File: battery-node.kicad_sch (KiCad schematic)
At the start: 20 parts, among them J2 Conn_01x02, J3 Conn_01x02, J7 TC2050, U1 ESP32-H2-MINI-1-H2S

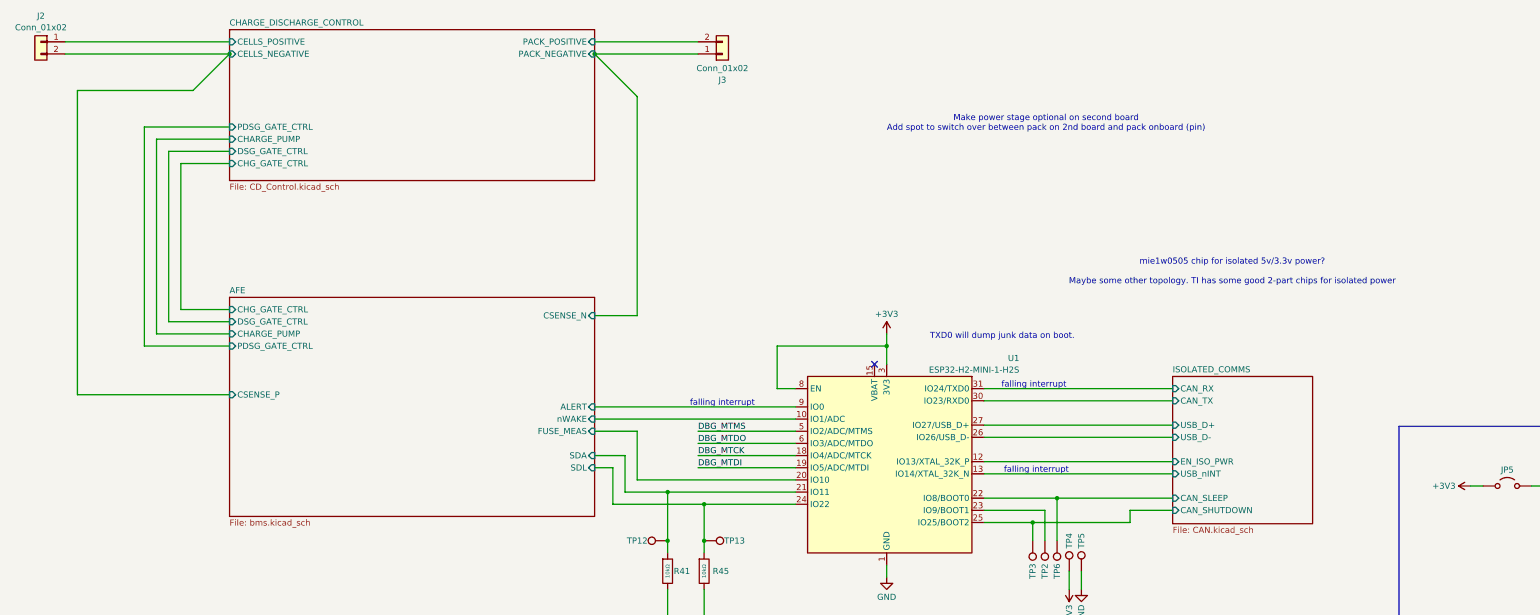
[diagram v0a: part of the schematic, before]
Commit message: prepping for split into 2 boards
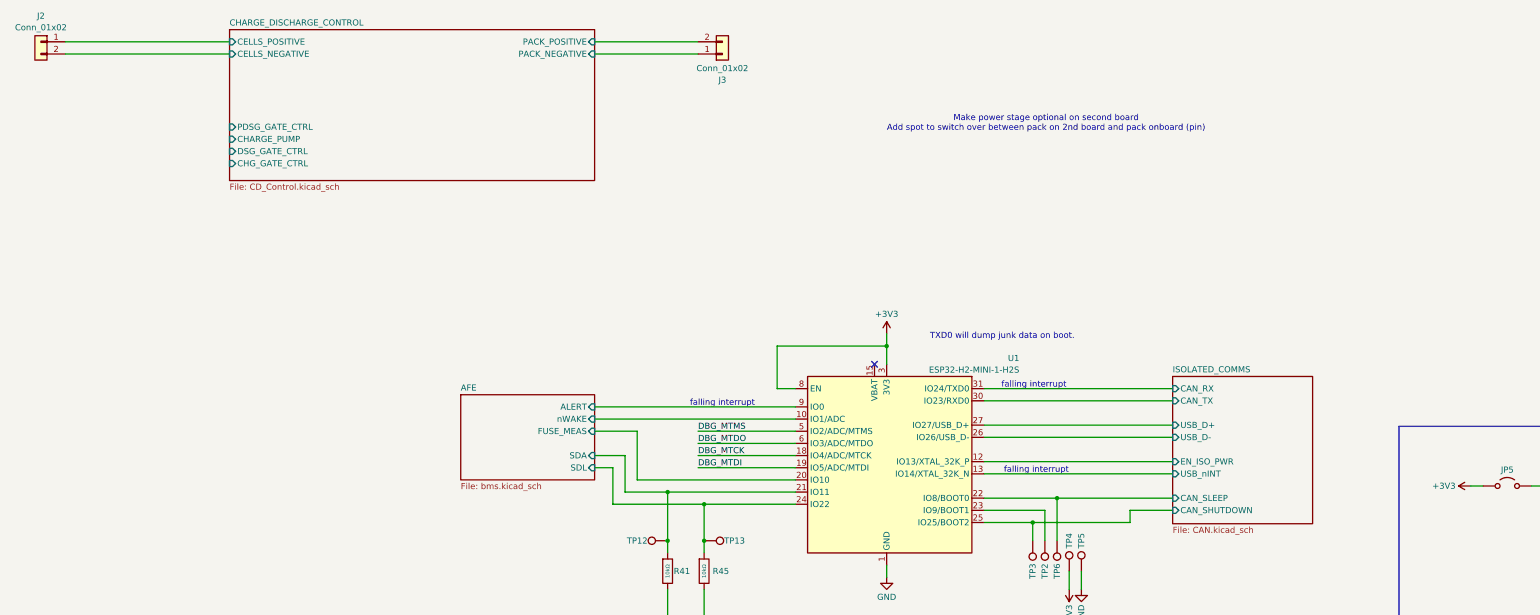
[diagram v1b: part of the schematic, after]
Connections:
- net AFE/CSENSE_N renamed CHARGE_DISCHARGE_CONTROL/PACK_NEGATIVE
- net AFE/CSENSE_P renamed CHARGE_DISCHARGE_CONTROL/CELLS_NEGATIVE
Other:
- sheet AFE ports: added none; removed CHARGE_PUMP, CHG_GATE_CTRL, CSENSE_N, CSENSE_P, DSG_GATE_CTRL, PDSG_GATE_CTRL
- note removed: "mie1w0505 chip for isolated 5v/3.3v power? Maybe some other topology. TI has some good 2-part chips for isolated power"
